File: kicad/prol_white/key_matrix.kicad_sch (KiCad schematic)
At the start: 114 parts, among them SW1 SW_Push_45deg, SW10 SW_Push_45deg, SW100 SW_Push_45deg, SW101 SW_Push_45deg, SW102 SW_Push_45deg, SW103 SW_Push_45deg, SW104 SW_Push_45deg, SW105 SW_Push_45deg, SW106 SW_Push_45deg, SW107 SW_Push_45deg, SW108 SW_Push_45deg, SW109 SW_Push_45deg, SW11 SW_Push_45deg, SW110 SW_Push_45deg, SW111 SW_Push_45deg, SW112 SW_Push_45deg, SW113 SW_Push_45deg, SW114 SW_Push_45deg, SW12 SW_Push_45deg, SW13 SW_Push_45deg, SW14 SW_Push_45deg, SW15 SW_Push_45deg, SW16 SW_Push_45deg, SW17 SW_Push_45deg, SW18 SW_Push_45deg, SW19 SW_Push_45deg, SW2 SW_Push_45deg, SW20 SW_Push_45deg, SW21 SW_Push_45deg, SW22 SW_Push_45deg, SW23 SW_Push_45deg, SW24 SW_Push_45deg, SW25 SW_Push_45deg, SW26 SW_Push_45deg, SW27 SW_Push_45deg, SW28 SW_Push_45deg, SW29 SW_Push_45deg, SW3 SW_Push_45deg, SW30 SW_Push_45deg, SW31 SW_Push_45deg, SW32 SW_Push_45deg, SW33 SW_Push_45deg, SW34 SW_Push_45deg, SW35 SW_Push_45deg, SW36 SW_Push_45deg, SW37 SW_Push_45deg, SW38 SW_Push_45deg, SW39 SW_Push_45deg, SW4 SW_Push_45deg, SW40 SW_Push_45deg, SW41 SW_Push_45deg, SW42 SW_Push_45deg, SW43 SW_Push_45deg, SW44 SW_Push_45deg, SW45 SW_Push_45deg, SW46 SW_Push_45deg, SW47 SW_Push_45deg, SW48 SW_Push_45deg, SW49 SW_Push_45deg, SW5 SW_Push_45deg, SW50 SW_Push_45deg, SW51 SW_Push_45deg, SW52 SW_Push_45deg, SW53 SW_Push_45deg, SW54 SW_Push_45deg, SW55 SW_Push_45deg, SW56 SW_Push_45deg, SW57 SW_Push_45deg, SW58 SW_Push_45deg, SW59 SW_Push_45deg, SW6 SW_Push_45deg, SW60 SW_Push_45deg, SW61 SW_Push_45deg, SW62 SW_Push_45deg, SW63 SW_Push_45deg, SW64 SW_Push_45deg, SW65 SW_Push_45deg, SW66 SW_Push_45deg, SW67 SW_Push_45deg, SW68 SW_Push_45deg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

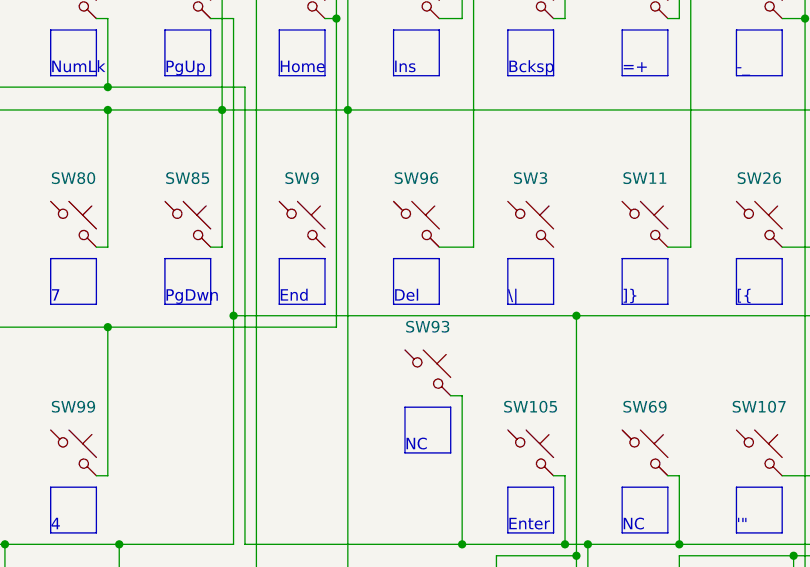
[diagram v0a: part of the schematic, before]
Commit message: kicad/prol_white: add missing key-row connections
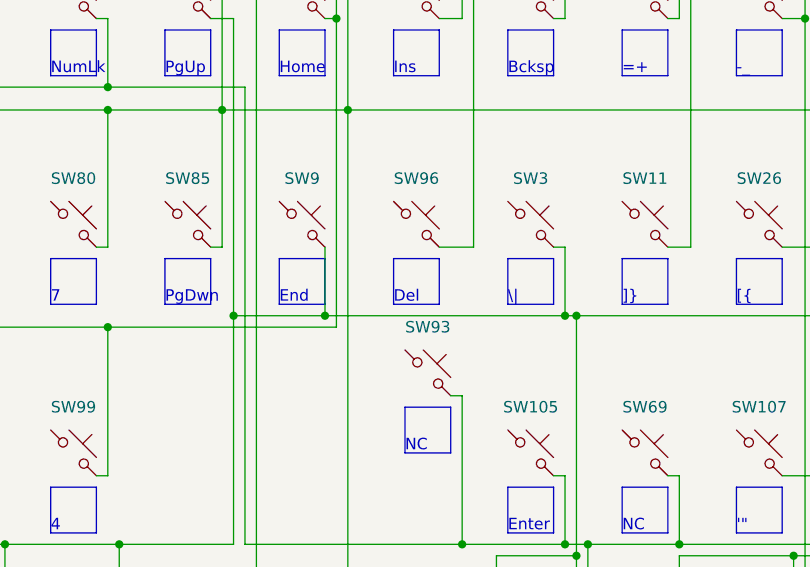
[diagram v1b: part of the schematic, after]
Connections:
- net KEY_ROW3: now also SW3.2, SW9.2
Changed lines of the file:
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@@
   (junction (at 172.72 68.58) (diameter 0) (color 0 0 0 0)
   )
+  (junction (at 82.55 91.44) (diameter 0) (color 0 0 0 0)
+  )
   (junction (at 160.02 116.84) (diameter 0) (color 0 0 0 0)
   )
@@
   (junction (at 198.12 48.26) (diameter 0) (color 0 0 0 0)
   )
+  (junction (at 109.22 91.44) (diameter 0) (color 0 0 0 0)
+  )
   (junction (at 236.22 43.18) (diameter 0) (color 0 0 0 0)
   )
@@
     (stroke (width 0) (type default) (color 0 0 0 0))
   )
+  (wire (pts (xy 109.22 83.82) (xy 109.22 91.44))
+    (stroke (width 0) (type default) (color 0 0 0 0))
+  )
   (polyline (pts (xy 102.87 161.29) (xy 107.95 161.29))
     (stroke (width 0) (type default) (color 0 0 0 0))
@@
     (stroke (width 0) (type default) (color 0 0 0 0))
   )
+  (wire (pts (xy 107.95 83.82) (xy 109.22 83.82))
+    (stroke (width 0) (type default) (color 0 0 0 0))
+  )
   (wire (pts (xy 210.82 43.18) (xy 210.82 58.42))
     (stroke (width 0) (type default) (color 0 0 0 0))
@@
     (stroke (width 0) (type default) (color 0 0 0 0))
   )
+  (wire (pts (xy 82.55 83.82) (xy 82.55 91.44))
+    (stroke (width 0) (type default) (color 0 0 0 0))
+  )
   (polyline (pts (xy 128.27 85.09) (xy 133.35 85.09))
     (stroke (width 0) (type default) (color 0 0 0 0))
@@
     (stroke (width 0) (type default) (color 0 0 0 0))
   )
+  (wire (pts (xy 82.55 91.44) (xy 109.22 91.44))
+    (stroke (width 0) (type default) (color 0 0 0 0))
+  )
   (polyline (pts (xy 255.27 85.09) (xy 260.35 85.09))
     (stroke (width 0) (type default) (color 0 0 0 0))
@@
     (stroke (width 0) (type default) (color 0 0 0 0))
   )
+  (wire (pts (xy 109.22 91.44) (xy 110.49 91.44))
+    (stroke (width 0) (type default) (color 0 0 0 0))
+  )
   (polyline (pts (xy 191.77 39.37) (xy 191.77 34.29))
     (stroke (width 0) (type default) (color 0 0 0 0))
@@
     (stroke (width 0) (type default) (color 0 0 0 0))
   )
-  (wire (pts (xy 72.39 91.44) (xy 110.49 91.44))
-    (stroke (width 0) (type default) (color 0 0 0 0))
-  )
+  (wire (pts (xy 72.39 91.44) (xy 82.55 91.44))
+    (stroke (width 0) (type default) (color 0 0 0 0))
+  )

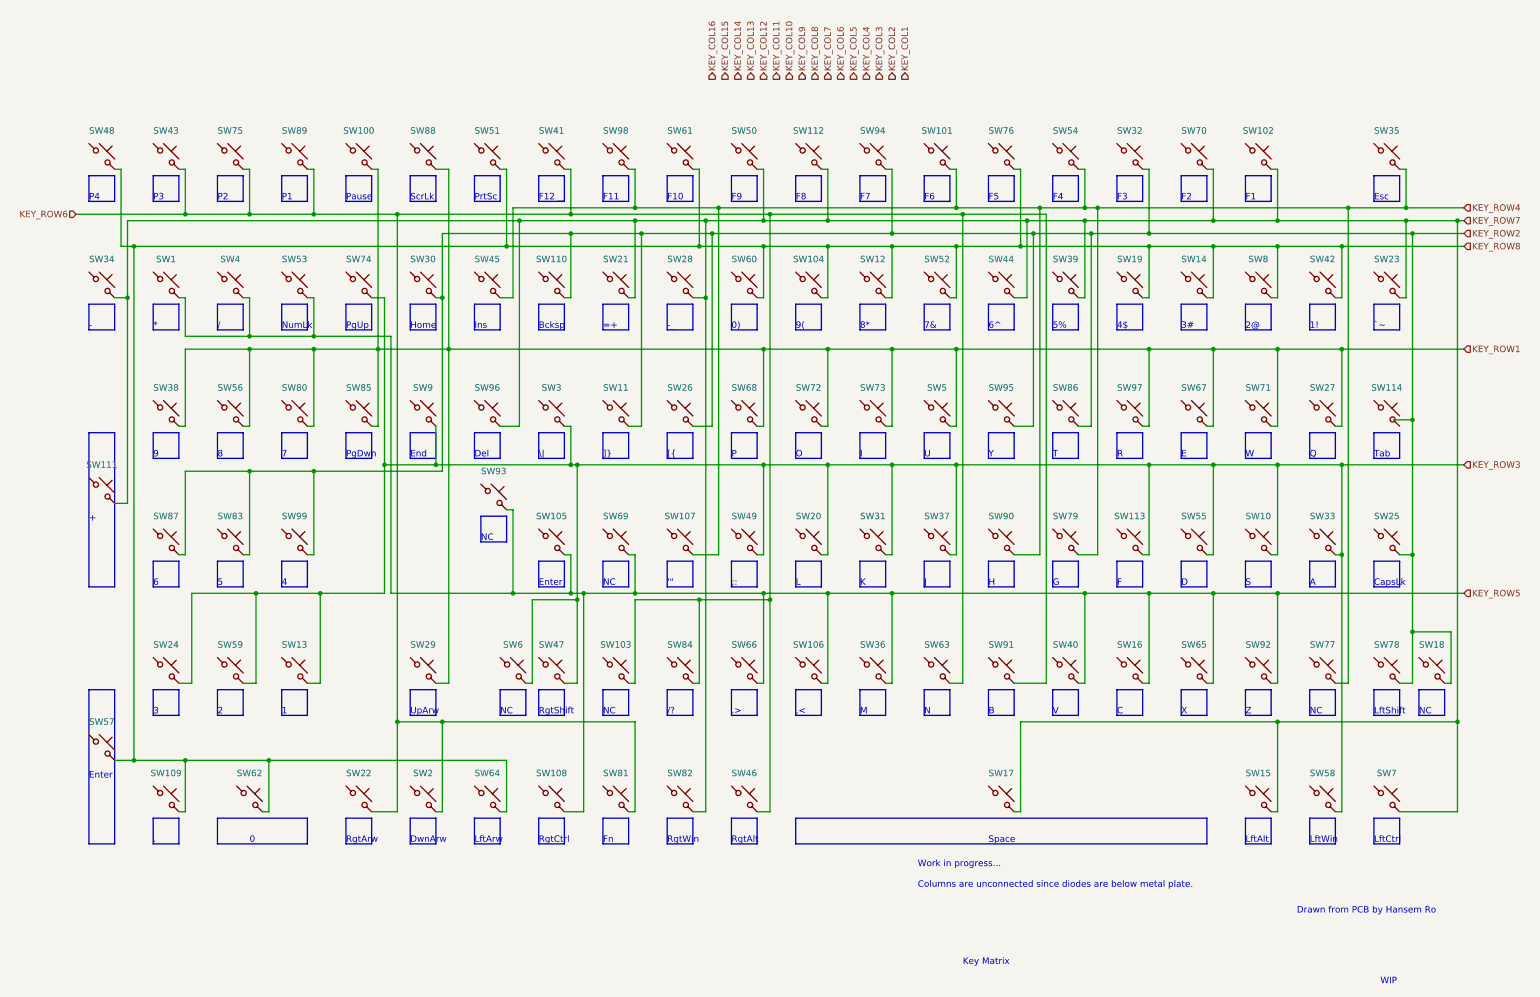
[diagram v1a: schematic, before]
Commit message: kicad/prol_white: finish key matrix sheet
Used QMK debug logging to complete key matrix.
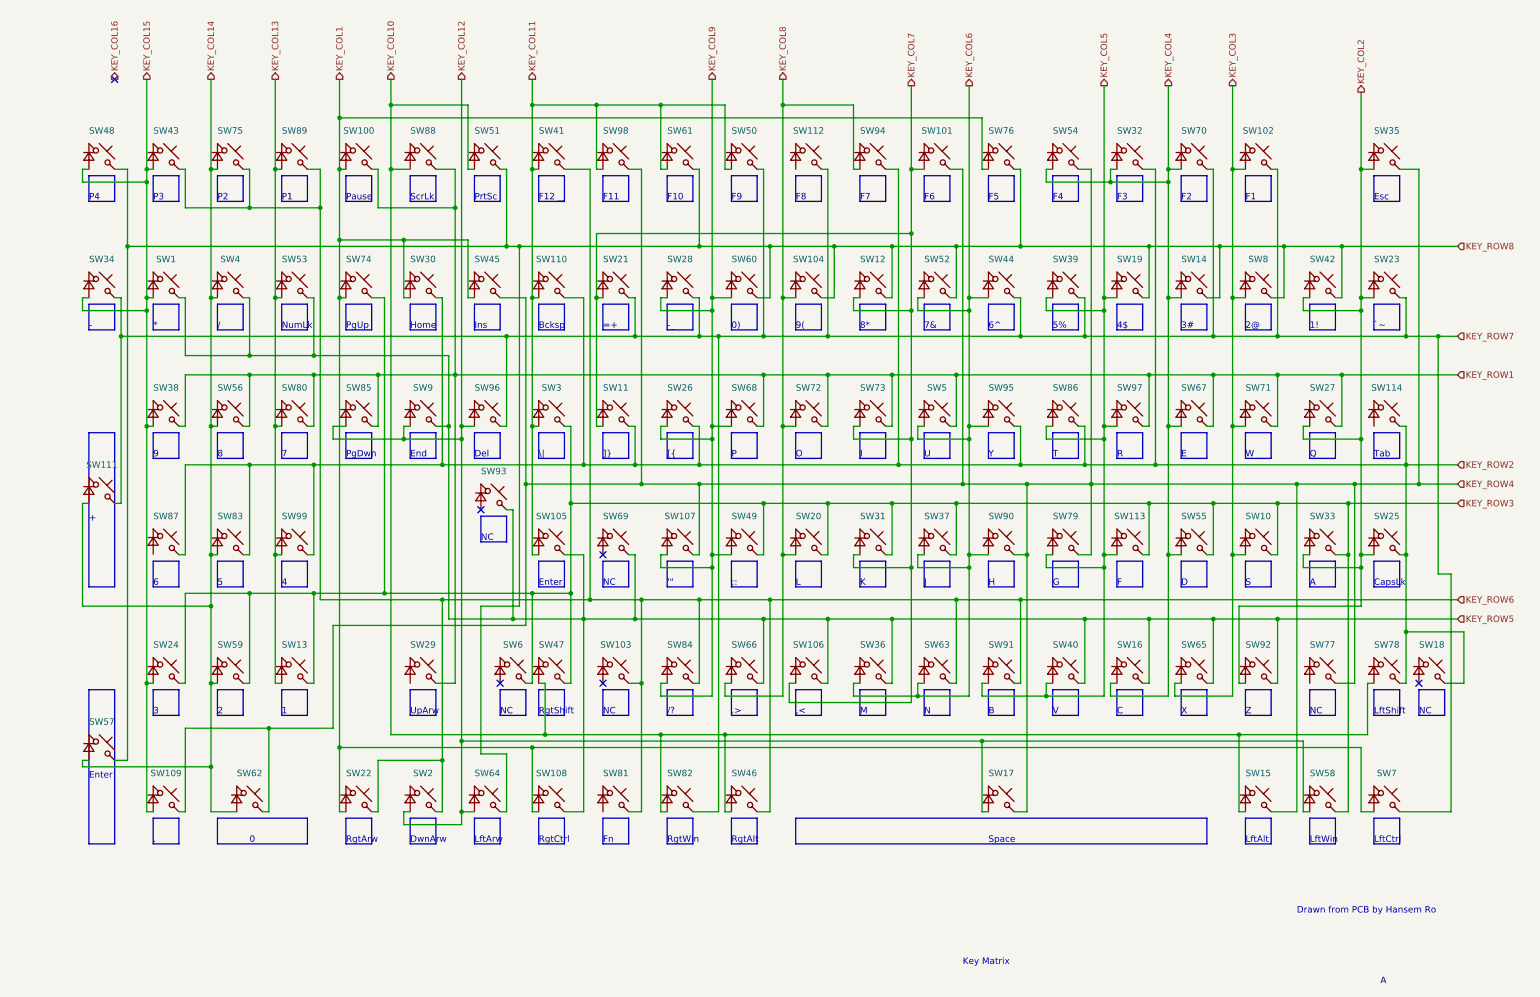
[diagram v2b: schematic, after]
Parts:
- added D? (x114): D_Small, symbol Device:D_Small
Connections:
- net KEY_COL1: now also D?.2 (A), D?.2 (A), D?.2 (A), D?.2 (A), D?.2 (A), D?.2 (A), D?.2 (A), D?.2 (A)
- net KEY_COL10: now also D?.2 (A), D?.2 (A), D?.2 (A), D?.2 (A), D?.2 (A), D?.2 (A), D?.2 (A)
- net KEY_COL11: now also D?.2 (A), D?.2 (A), D?.2 (A), D?.2 (A), D?.2 (A), D?.2 (A), D?.2 (A)
- net KEY_COL12: now also D?.2 (A), D?.2 (A), D?.2 (A), D?.2 (A), D?.2 (A), D?.2 (A), D?.2 (A)
- net KEY_COL13: now also D?.2 (A), D?.2 (A), D?.2 (A), D?.2 (A), D?.2 (A)
- net KEY_COL14: now also D?.2 (A), D?.2 (A), D?.2 (A), D?.2 (A), D?.2 (A), D?.2 (A), D?.2 (A), D?.2 (A)
- net KEY_COL15: now also D?.2 (A), D?.2 (A), D?.2 (A), D?.2 (A), D?.2 (A), D?.2 (A), D?.2 (A)
- net KEY_COL2: now also D?.2 (A), D?.2 (A), D?.2 (A), D?.2 (A), D?.2 (A), D?.2 (A), D?.2 (A)
- net KEY_COL3: now also D?.2 (A), D?.2 (A), D?.2 (A), D?.2 (A), D?.2 (A)
- net KEY_COL4: now also D?.2 (A), D?.2 (A), D?.2 (A), D?.2 (A), D?.2 (A), D?.2 (A), D?.2 (A)
- net KEY_COL5: now also D?.2 (A), D?.2 (A), D?.2 (A), D?.2 (A), D?.2 (A), D?.2 (A), D?.2 (A), D?.2 (A)
- net KEY_COL6: now also D?.2 (A), D?.2 (A), D?.2 (A), D?.2 (A), D?.2 (A), D?.2 (A), D?.2 (A), D?.2 (A)
- net KEY_COL7: now also D?.2 (A), D?.2 (A), D?.2 (A), D?.2 (A), D?.2 (A), D?.2 (A), D?.2 (A)
- net KEY_COL8: now also D?.2 (A), D?.2 (A), D?.2 (A), D?.2 (A), D?.2 (A)
- net KEY_COL9: now also D?.2 (A), D?.2 (A), D?.2 (A), D?.2 (A), D?.2 (A), D?.2 (A), D?.2 (A)
- net KEY_ROW2: now also SW114.2
- net KEY_ROW3: no longer SW9.2
- net KEY_ROW4: now also SW109.2, SW15.2, SW17.2, SW62.2
- net KEY_ROW5: now also SW9.2
- net KEY_ROW7: no longer SW15.2, SW17.2
- net KEY_ROW8: no longer SW109.2, SW62.2
- net at SW1.1: now also D?.1 (K)
- net at SW2.1: now also D?.1 (K)
- net at SW3.1: now also D?.1 (K)
- net at SW4.1: now also D?.1 (K)
- net at SW5.1: now also D?.1 (K)
- net at SW6.1: now also D?.1 (K)
- net at SW7.1: now also D?.1 (K)
- net at SW8.1: now also D?.1 (K)
- net at SW9.1: now also D?.1 (K)
- net at SW10.1: now also D?.1 (K)
- net at SW11.1: now also D?.1 (K)
- net at SW12.1: now also D?.1 (K)
- net at SW13.1: now also D?.1 (K)
- net at SW14.1: now also D?.1 (K)
- net at SW15.1: now also D?.1 (K)
- net at SW16.1: now also D?.1 (K)
- net at SW17.1: now also D?.1 (K)
- net at SW18.1: now also D?.1 (K)
- net at SW19.1: now also D?.1 (K)
- net at SW20.1: now also D?.1 (K)
- net at SW21.1: now also D?.1 (K)
- net at SW22.1: now also D?.1 (K)
- net at SW23.1: now also D?.1 (K)
- net at SW24.1: now also D?.1 (K)
- net at SW25.1: now also D?.1 (K)
- net at SW26.1: now also D?.1 (K)
- net at SW27.1: now also D?.1 (K)
- net at SW28.1: now also D?.1 (K)
- net at SW29.1: now also D?.1 (K)
- net at SW30.1: now also D?.1 (K)
- net at SW31.1: now also D?.1 (K)
- net at SW32.1: now also D?.1 (K)
- net at SW33.1: now also D?.1 (K)
- net at SW34.1: now also D?.1 (K)
- net at SW35.1: now also D?.1 (K)
- net at SW36.1: now also D?.1 (K)
- net at SW37.1: now also D?.1 (K)
- net at SW38.1: now also D?.1 (K)
- net at SW39.1: now also D?.1 (K)
- net at SW40.1: now also D?.1 (K)
- net at SW41.1: now also D?.1 (K)
- net at SW42.1: now also D?.1 (K)
- net at SW43.1: now also D?.1 (K)
- net at SW44.1: now also D?.1 (K)
- net at SW45.1: now also D?.1 (K)
- net at SW46.1: now also D?.1 (K)
- net at SW47.1: now also D?.1 (K)
- net at SW48.1: now also D?.1 (K)
- net at SW49.1: now also D?.1 (K)
- net at SW50.1: now also D?.1 (K)
- net at SW51.1: now also D?.1 (K)
- net at SW52.1: now also D?.1 (K)
- net at SW53.1: now also D?.1 (K)
- net at SW54.1: now also D?.1 (K)
- net at SW55.1: now also D?.1 (K)
- net at SW56.1: now also D?.1 (K)
- net at SW57.1: now also D?.1 (K)
- net at SW58.1: now also D?.1 (K)
- net at SW59.1: now also D?.1 (K)
- net at SW60.1: now also D?.1 (K)
- net at SW61.1: now also D?.1 (K)
- net at SW62.1: now also D?.1 (K)
- net at SW63.1: now also D?.1 (K)
- net at SW64.1: now also D?.1 (K)
- net at SW65.1: now also D?.1 (K)
- net at SW66.1: now also D?.1 (K)
- net at SW67.1: now also D?.1 (K)
- net at SW68.1: now also D?.1 (K)
- net at SW69.1: now also D?.1 (K)
- net at SW70.1: now also D?.1 (K)
- net at SW71.1: now also D?.1 (K)
- net at SW72.1: now also D?.1 (K)
- net at SW73.1: now also D?.1 (K)
- net at SW74.1: now also D?.1 (K)
- net at SW75.1: now also D?.1 (K)
- net at SW76.1: now also D?.1 (K)
- net at SW77.1: now also D?.1 (K)
- net at SW78.1: now also D?.1 (K)
- net at SW79.1: now also D?.1 (K)
- net at SW80.1: now also D?.1 (K)
- net at SW81.1: now also D?.1 (K)
- net at SW82.1: now also D?.1 (K)
- net at SW83.1: now also D?.1 (K)
- net at SW84.1: now also D?.1 (K)
- net at SW85.1: now also D?.1 (K)
- net at SW86.1: now also D?.1 (K)
- net at SW88.1: now also D?.1 (K)
- net at SW89.1: now also D?.1 (K)
- net at SW90.1: now also D?.1 (K)
- net at SW91.1: now also D?.1 (K)
- net at SW92.1: now also D?.1 (K)
- net at SW93.1: now also D?.1 (K)
- net at SW94.1: now also D?.1 (K)
- net at SW95.1: now also D?.1 (K)
- net at SW96.1: now also D?.1 (K)
- net at SW97.1: now also D?.1 (K)
- net at SW98.1: now also D?.1 (K)
- net at SW99.1: now also D?.1 (K)
- net at SW100.1: now also D?.1 (K)
- net at SW101.1: now also D?.1 (K)
- net at SW102.1: now also D?.1 (K)
- net at SW103.1: now also D?.1 (K)
- net at SW104.1: now also D?.1 (K)
- net at SW105.1: now also D?.1 (K)
- net at SW106.1: now also D?.1 (K)
- net at SW107.1: now also D?.1 (K)
- net at SW108.1: now also D?.1 (K)
- net at SW109.1: now also D?.1 (K)
- net at SW110.1: now also D?.1 (K)
- net at SW111.1: now also D?.1 (K)
- net at SW112.1: now also D?.1 (K)
- net at SW113.1: now also D?.1 (K)
- net at SW114.1: now also D?.1 (K)
- no-connect marks 0 -> 6
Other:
- note removed: "WIP"
- note removed: "Work in progress... Columns are unconnected since diodes are below metal plate."
